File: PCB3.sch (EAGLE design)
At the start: 48 parts

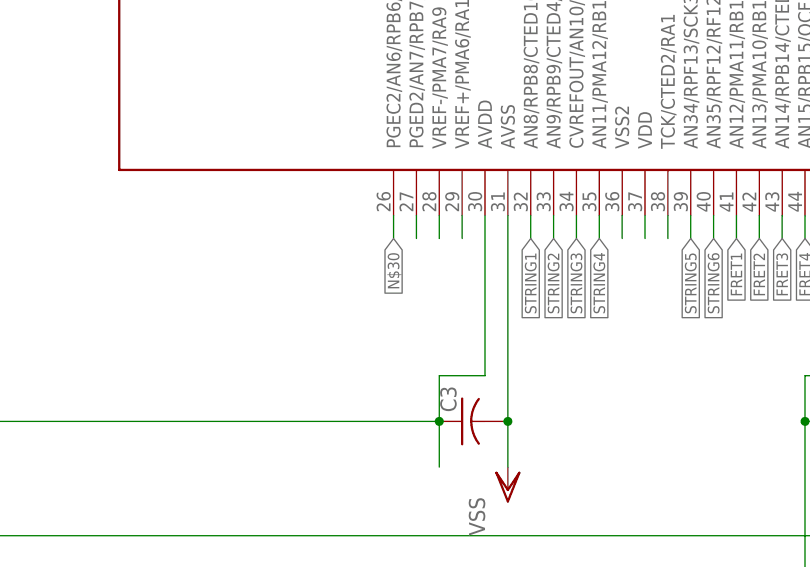
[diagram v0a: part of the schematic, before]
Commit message: Added oscillator schematic to Stamp Board and started layout corrections.
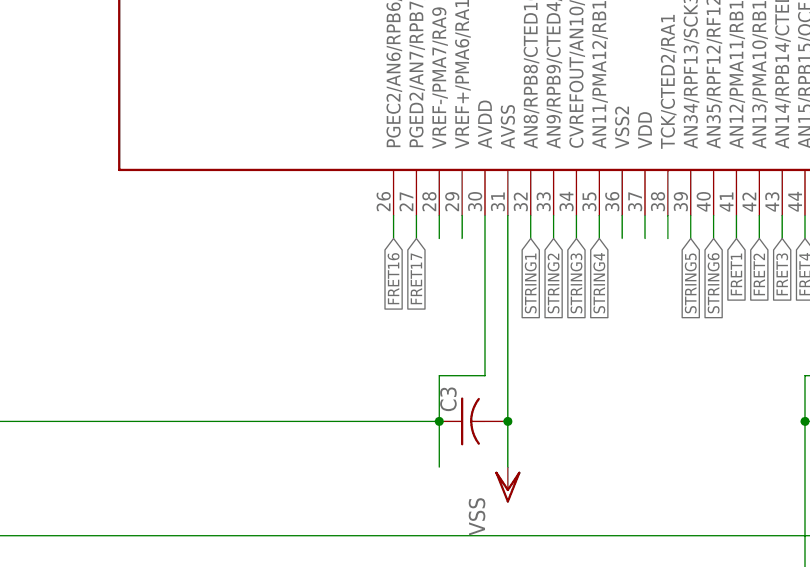
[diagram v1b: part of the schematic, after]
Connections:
- net N$30 renamed FRET16
- net N$43 renamed FRET17
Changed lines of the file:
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@@
 </segment>
 </net>
-<net name="N$43" class="0">
+<net name="FRET17" class="0">
 <segment>
 <wire x1="111.76" y1="53.34" x2="111.76" y2="50.8" width="0.1524" layer="91"/>
 <pinref part="U$2" gate="G$1" pin="PGED2/AN7/RPB7/CTED3/RB7"/>
+<label x="111.76" y="50.8" size="1.27" layer="95" rot="R270" xref="yes"/>
 </segment>
 </net>
@@
 </segment>
 </net>
-<net name="N$30" class="0">
+<net name="FRET16" class="0">
 <segment>
 <pinref part="R8" gate="G$1" pin="1"/>

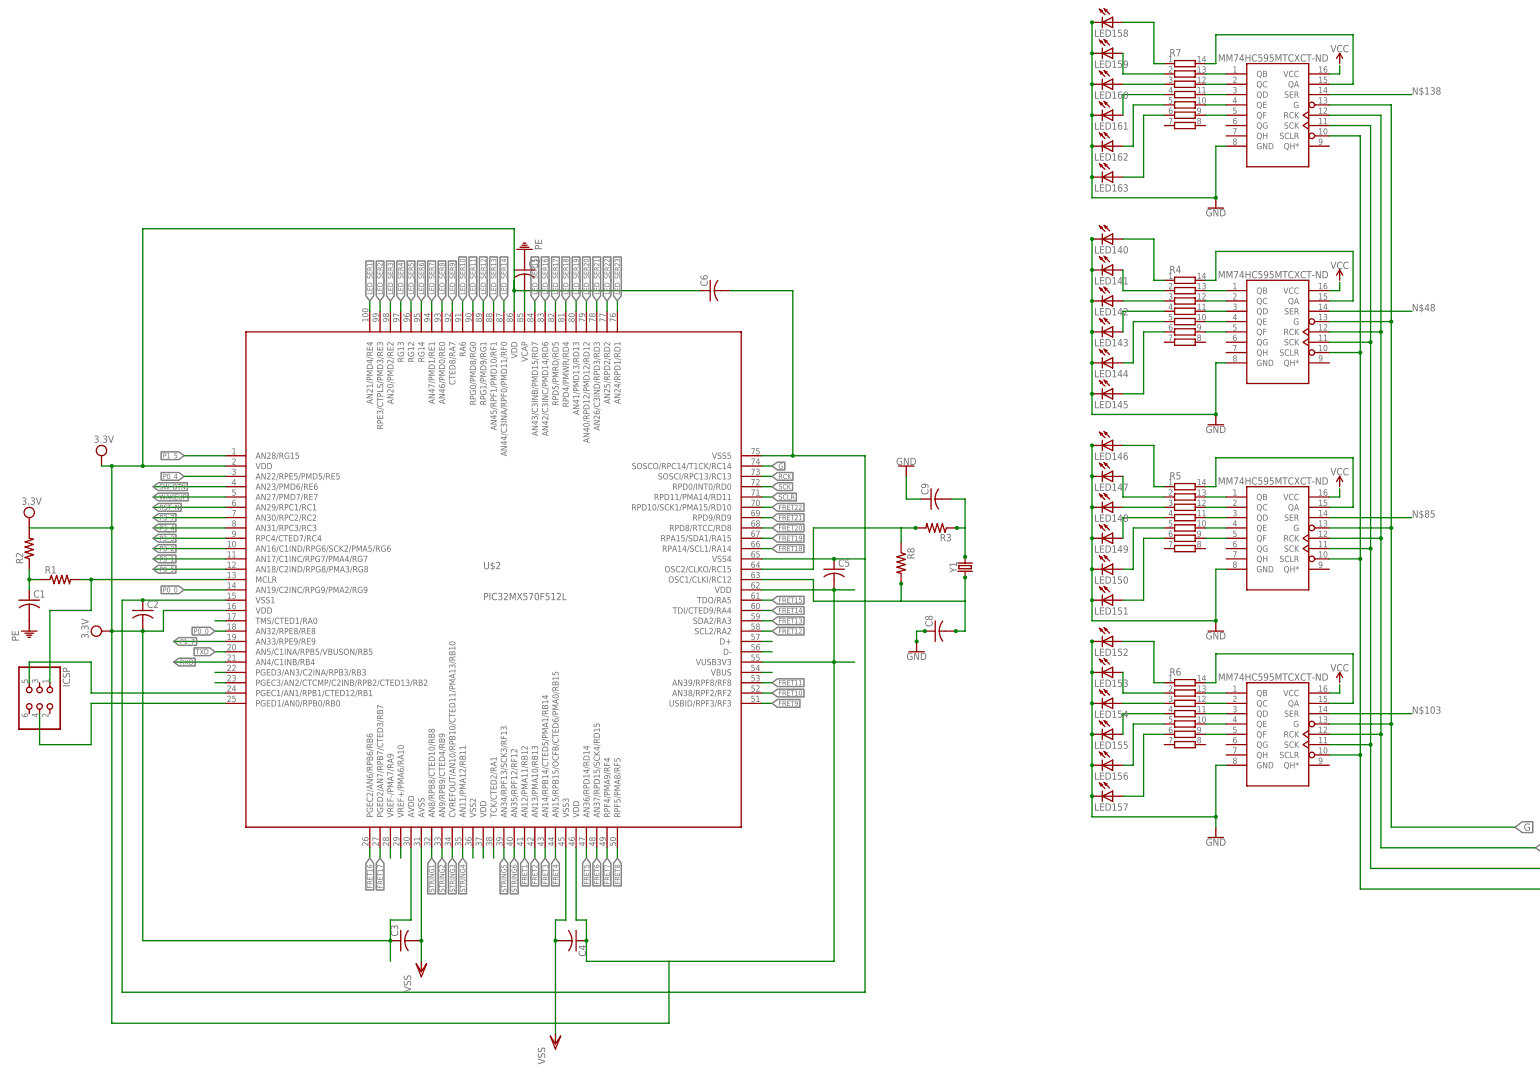
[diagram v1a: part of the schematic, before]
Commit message: Changed most pins on micro and condensed all of the connections on PCB3. Began making traces for other PCBs from PCB3 and created GRN plane for PCB3.
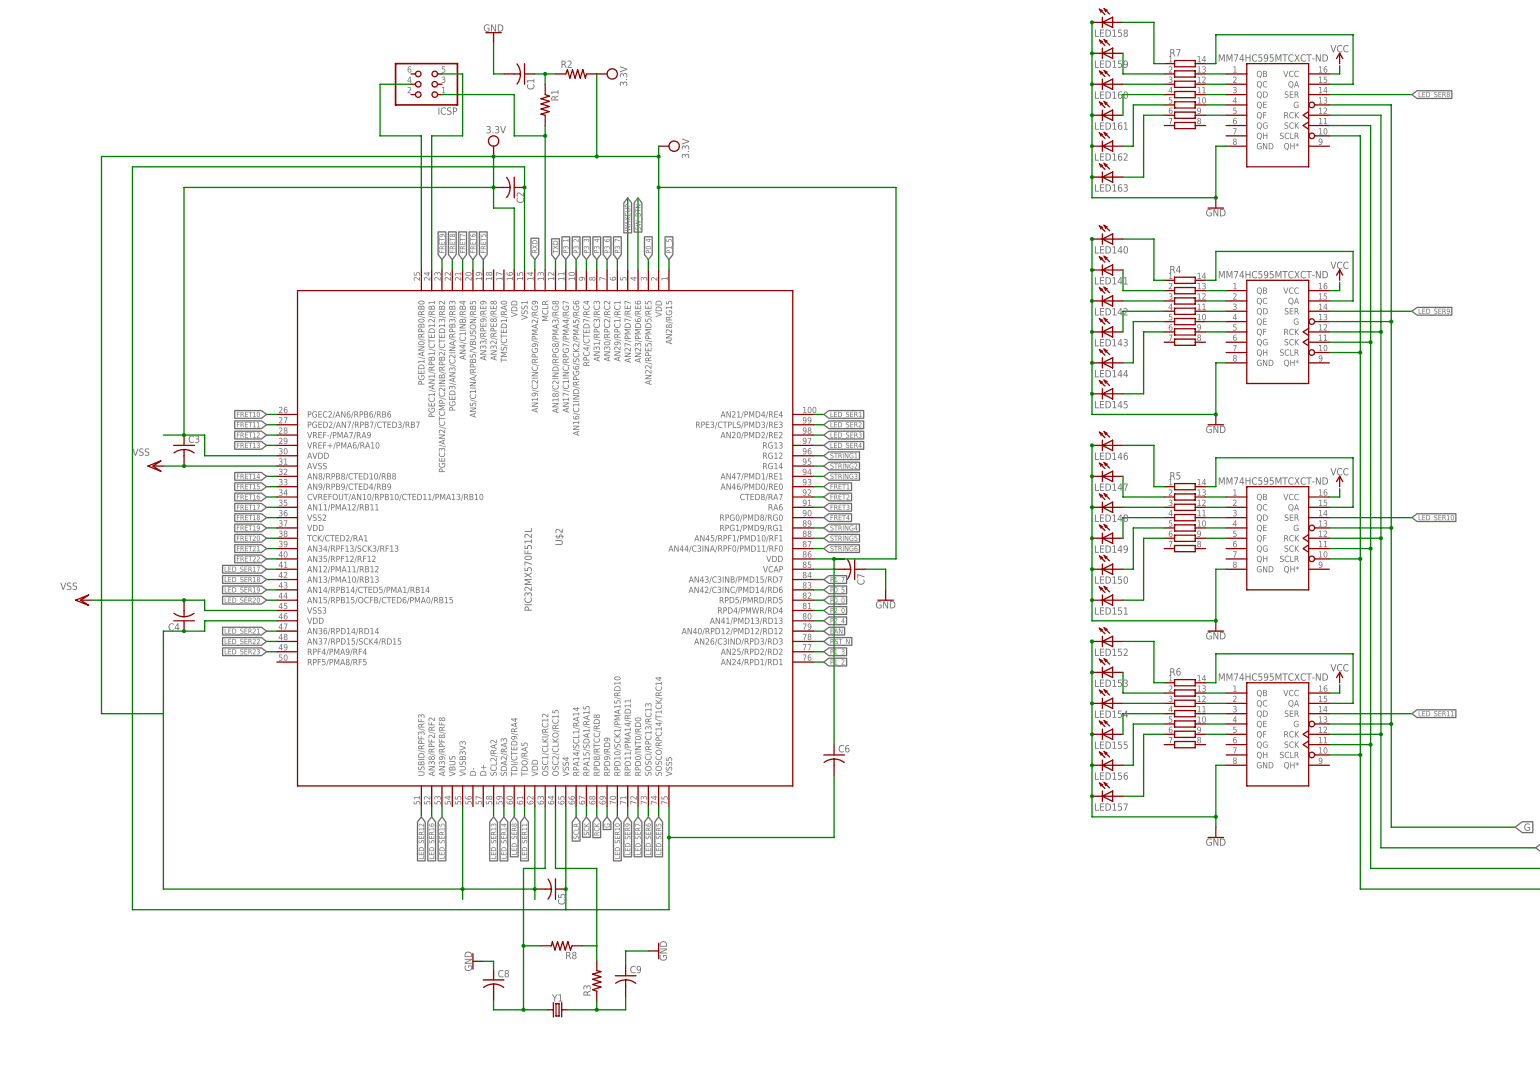
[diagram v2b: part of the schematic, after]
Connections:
- removed net N$103: U$29.SER
- removed net N$138: U$26.SER
- removed net N$3: U$2.TMS/CTED1/RA0
- removed net N$4: U$2.PGED3/AN3/C2INA/RPB3/RB3
- removed net N$42: U$2.PGEC2/AN6/RPB6/RB6
- removed net N$44: U$2.VREF-/PMA7/RA9
- removed net N$45: U$2.VREF+/PMA6/RA10
- removed net N$48: U$27.SER
- removed net N$5: U$2.PGEC3/AN2/CTCMP/C2INB/RPB2/CTED13/RB2
- removed net N$50: U$2.VSS2
- removed net N$51: U$2.VDD@2
- removed net N$52: U$2.TCK/CTED2/RA1
- removed net N$66: U$2.VBUS
- removed net N$67: U$2.D-
- removed net N$68: U$2.D+
- removed net N$85: U$28.SER
- removed net PE: C1.2, C7.1
- new net EAN: U$2.AN40/RPD12/PMD12/RD12
- new net OSC2: R3.2, R8.1, U$2.OSC2/CLKO/RC15
- new net P1_2: U$2.AN24/RPD1/RD1
- new net P1_3: U$2.AN25/RPD2/RD2
- new net P2_0: U$2.RPD4/PMWR/RD4
- new net P2_4: U$2.AN41/PMD13/RD13
- new net P3_6: U$2.AN30/RPC2/RC2
- net FRET1: now also U$2.AN46/PMD0/RE0; no longer U$2.AN12/PMA11/RB12
- net FRET10: now also U$2.PGEC2/AN6/RPB6/RB6; no longer U$2.AN38/RPF2/RF2
- net FRET11: now also U$2.PGED2/AN7/RPB7/CTED3/RB7; no longer U$2.AN39/RPF8/RF8
- net FRET12: now also U$2.VREF-/PMA7/RA9; no longer U$2.SCL2/RA2
- net FRET13: now also U$2.VREF+/PMA6/RA10; no longer U$2.SDA2/RA3
- net FRET14: now also U$2.AN8/RPB8/CTED10/RB8; no longer U$2.TDI/CTED9/RA4
- net FRET15: now also U$2.AN9/RPB9/CTED4/RB9; no longer U$2.TDO/RA5
- net FRET16: now also U$2.CVREFOUT/AN10/RPB10/CTED11/PMA13/RB10; no longer R3.2, R8.1, U$2.OSC2/CLKO/RC15
- net FRET17: now also U$2.AN11/PMA12/RB11; no longer U$2.PGED2/AN7/RPB7/CTED3/RB7
- net FRET18: now also U$2.VSS2; no longer U$2.RPA14/SCL1/RA14
- net FRET19: now also U$2.VDD@2; no longer U$2.RPA15/SDA1/RA15
- net FRET2: now also U$2.CTED8/RA7; no longer U$2.AN13/PMA10/RB13
- net FRET20: now also U$2.TCK/CTED2/RA1; no longer U$2.RPD8/RTCC/RD8
- net FRET21: now also U$2.AN34/RPF13/SCK3/RF13; no longer U$2.RPD9/RD9
- net FRET22: now also U$2.AN35/RPF12/RF12; no longer U$2.RPD10/SCK1/PMA15/RD10
- net FRET3: now also U$2.RA6; no longer U$2.AN14/RPB14/CTED5/PMA1/RB14
- net FRET4: now also U$2.RPG0/PMD8/RG0; no longer U$2.AN15/RPB15/OCFB/CTED6/PMA0/RB15
- net FRET5: now also U$2.AN33/RPE9/RE9; no longer U$2.AN36/RPD14/RD14
- net FRET6: now also U$2.AN5/C1INA/RPB5/VBUSON/RB5; no longer U$2.AN37/RPD15/SCK4/RD15
- net FRET7: now also U$2.AN4/C1INB/RB4; no longer U$2.RPF4/PMA9/RF4
- net FRET8: now also U$2.PGED3/AN3/C2INA/RPB3/RB3; no longer U$2.RPF5/PMA8/RF5
- net FRET9: now also U$2.PGEC3/AN2/CTCMP/C2INB/RPB2/CTED13/RB2; no longer U$2.USBID/RPF3/RF3
- net G: now also U$2.RPD9/RD9; no longer U$2.SOSCO/RPC14/T1CK/RC14
- net GND: now also C1.2, C7.1
- net LED_SER10: now also U$2.RPD10/SCK1/PMA15/RD10, U$28.SER; no longer U$2.RA6
- net LED_SER11: now also U$2.TDO/RA5, U$29.SER; no longer U$2.RPG0/PMD8/RG0
- net LED_SER12: now also U$2.USBID/RPF3/RF3; no longer U$2.RPG1/PMD9/RG1
- net LED_SER13: now also U$2.SCL2/RA2; no longer U$2.AN45/RPF1/PMD10/RF1
- net LED_SER14: now also U$2.SDA2/RA3; no longer U$2.AN44/C3INA/RPF0/PMD11/RF0
- net LED_SER15: now also U$2.AN39/RPF8/RF8; no longer U$2.AN43/C3INB/PMD15/RD7
- net LED_SER16: now also U$2.AN38/RPF2/RF2; no longer U$2.AN42/C3INC/PMD14/RD6
- net LED_SER17: now also U$2.AN12/PMA11/RB12; no longer U$2.RPD5/PMRD/RD5
- net LED_SER18: now also U$2.AN13/PMA10/RB13; no longer U$2.RPD4/PMWR/RD4
- net LED_SER19: now also U$2.AN14/RPB14/CTED5/PMA1/RB14; no longer U$2.AN41/PMD13/RD13
- net LED_SER20: now also U$2.AN15/RPB15/OCFB/CTED6/PMA0/RB15; no longer U$2.AN40/RPD12/PMD12/RD12
- net LED_SER21: now also U$2.AN36/RPD14/RD14; no longer U$2.AN26/C3IND/RPD3/RD3
- net LED_SER22: now also U$2.AN37/RPD15/SCK4/RD15; no longer U$2.AN25/RPD2/RD2
- net LED_SER23: now also U$2.RPF4/PMA9/RF4; no longer U$2.AN24/RPD1/RD1
- net LED_SER5: now also U$2.SOSCO/RPC14/T1CK/RC14; no longer U$2.RG12
- net LED_SER6: now also U$2.SOSCI/RPC13/RC13; no longer U$2.RG14
- net LED_SER7: now also U$2.RPD0/INT0/RD0; no longer U$2.AN47/PMD1/RE1
- net LED_SER8: now also U$2.TDI/CTED9/RA4, U$26.SER; no longer U$2.AN46/PMD0/RE0
- net LED_SER9: now also U$2.RPD11/PMA14/RD11, U$27.SER; no longer U$2.CTED8/RA7
- net P0_0: now also U$2.RPD5/PMRD/RD5; no longer U$2.AN19/C2INC/RPG9/PMA2/RG9, U$2.AN32/RPE8/RE8
- net P0_5: now also U$2.AN42/C3INC/PMD14/RD6; no longer U$2.AN18/C2IND/RPG8/PMA3/RG8
- net P1_7: now also U$2.AN43/C3INB/PMD15/RD7; no longer U$2.AN33/RPE9/RE9
- net P3_7: now also U$2.AN29/RPC1/RC1; no longer U$2.AN30/RPC2/RC2
- net RCK: now also U$2.RPD8/RTCC/RD8; no longer U$2.SOSCI/RPC13/RC13
- net RST_N: now also U$2.AN26/C3IND/RPD3/RD3; no longer U$2.AN29/RPC1/RC1
- net RXD: now also U$2.AN19/C2INC/RPG9/PMA2/RG9; no longer U$2.AN4/C1INB/RB4
- net SCK: now also U$2.RPA15/SDA1/RA15; no longer U$2.RPD0/INT0/RD0
- net SCLR: now also U$2.RPA14/SCL1/RA14; no longer U$2.RPD11/PMA14/RD11
- net STRING1: now also U$2.RG12; no longer U$2.AN8/RPB8/CTED10/RB8
- net STRING2: now also U$2.RG14; no longer U$2.AN9/RPB9/CTED4/RB9
- net STRING3: now also U$2.AN47/PMD1/RE1; no longer U$2.CVREFOUT/AN10/RPB10/CTED11/PMA13/RB10
- net STRING4: now also U$2.RPG1/PMD9/RG1; no longer U$2.AN11/PMA12/RB11
- net STRING5: now also U$2.AN45/RPF1/PMD10/RF1; no longer U$2.AN34/RPF13/SCK3/RF13
- net STRING6: now also U$2.AN44/C3INA/RPF0/PMD11/RF0; no longer U$2.AN35/RPF12/RF12
- net TXD: now also U$2.AN18/C2IND/RPG8/PMA3/RG8; no longer U$2.AN5/C1INA/RPB5/VBUSON/RB5
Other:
- moved on the sheet: C1, C2, C3, C4, C5, C6, C7, C8, C9, ICSP, R1, R2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
